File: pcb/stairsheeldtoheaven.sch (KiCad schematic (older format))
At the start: 29 parts

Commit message: schema complet
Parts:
- removed D?: LED, LEDs:LED-5MM, symbol LED-RESCUE-atxpowerboard
- removed P? (x16): CONN_01X02, symbol CONN_01X02
- removed R?: 220, Resistors_ThroughHole:Resistor_Horizontal_RM10mm, symbol R-RESCUE-atxpowerboard
- added P10, P11, P12, P13, P14, P15, P16, P17, P18, P19, P20, P21, P5, P6, P7, P8: CONN_01X02, symbol CONN_01X02
- gave numbers to parts that had none: 11
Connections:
- net A2 is gone; now on net 17: P22.2 (P2)
- net A3 is gone; now on net 18: P23.2 (P2)
- net A4 is gone; now on net 19: P24.2 (P2)
- net A5 is gone; now on net 20: P25.2 (P2)
- net 1: now also SHIELD1.0, P5.2 (P2)
- net 10: now also SHIELD1.9, P15.2 (P2)
- net 11: now also SHIELD1.10, P16.2 (P2)
- net 12: now also SHIELD1.11, P17.2 (P2)
- net 13: now also SHIELD1.12, P18.2 (P2)
- net 2: now also SHIELD1.1, P6.2 (P2)
- net 3: now also SHIELD1.2, P7.2 (P2)
- net 4: now also SHIELD1.3, P8.2 (P2)
- net 5: now also SHIELD1.4, P10.2 (P2)
- net 6: now also SHIELD1.5, P11.2 (P2)
- net 7: now also SHIELD1.6, P12.2 (P2)
- net 8: now also SHIELD1.7, P13.2 (P2)
- net 9: now also SHIELD1.8, P14.2 (P2)
- net GND: now also P22.1 (P1), P23.1 (P1), P24.1 (P1), P25.1 (P1), SHIELD1._GND (ICSP_GND), P10.1 (P1), P11.1 (P1), P12.1 (P1), P13.1 (P1), P14.1 (P1), P15.1 (P1), P16.1 (P1), P17.1 (P1), P18.1 (P1), P19.1 (P1), P20.1 (P1), P21.1 (P1), P5.1 (P1), P6.1 (P1), P7.1 (P1), P8.1 (P1)
- net clock: now also SHIELD1._SCK (ICSP_SCK)
- net data: now also SHIELD1._MOS (ICSP_MOSI)
- net 14: now reaches SHIELD1.13
- net 14: now also P19.2 (P2)
- net 15: now reaches SHIELD1.AD0
- net 15: now also P20.2 (P2)
- net 16: now reaches SHIELD1.AD1
- net 16: now also P21.2 (P2)
- net 17: now reaches SHIELD1.AD2
- net 18: now reaches SHIELD1.AD3
- net 19: now reaches SHIELD1.AD4
- net 20: now reaches SHIELD1.AD5
- net +5V renamed 5V_SB
- no-connect marks 2 -> 13
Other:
- moved on the sheet: P22, P23, P24, P25

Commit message: version1 PCB
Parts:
- JP1: footprint (none) -> Pin_Headers:Pin_Header_Straight_1x02
- P10: value CONN_01X02 -> 5; footprint (none) -> Connect:bornier2
- P11: value CONN_01X02 -> 6; footprint (none) -> Connect:bornier2
- P12: value CONN_01X02 -> 7; footprint (none) -> Connect:bornier2
- P13: value CONN_01X02 -> 8; footprint (none) -> Connect:bornier2
- P14: value CONN_01X02 -> 9; footprint (none) -> Connect:bornier2
- P15: value CONN_01X02 -> 10; footprint (none) -> Connect:bornier2
- P16: value CONN_01X02 -> 11; footprint (none) -> Connect:bornier2
- P17: value CONN_01X02 -> 12; footprint (none) -> Connect:bornier2
- P18: value CONN_01X02 -> 13; footprint (none) -> Connect:bornier2
- P19: value CONN_01X02 -> 14; footprint (none) -> Connect:bornier2
- P2: value 5V -> LED1
- P20: value CONN_01X02 -> 15; footprint (none) -> Connect:bornier2
- P21: value CONN_01X02 -> 16; footprint (none) -> Connect:bornier2
- P22: value CONN_01X02 -> 17; footprint (none) -> Connect:bornier2
- P23: value CONN_01X02 -> 18; footprint (none) -> Connect:bornier2
- P24: value CONN_01X02 -> 19; footprint (none) -> Connect:bornier2
- P25: value CONN_01X02 -> 20; footprint (none) -> Connect:bornier2
- P3: value 5V -> LED2
- P5: value CONN_01X02 -> 1; footprint (none) -> Connect:bornier2
- P6: value CONN_01X02 -> 2; footprint (none) -> Connect:bornier2
- P7: value CONN_01X02 -> 3; footprint (none) -> Connect:bornier2
- P8: value CONN_01X02 -> 4; footprint (none) -> Connect:bornier2
- SHIELD1: footprint (none) -> JbLb_lib:ARDUINO_SHIELD_R3
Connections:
- net GND: now also SHIELD1.GND3
- no-connect marks 13 -> 12
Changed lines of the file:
@@
 F 0 "SHIELD1" H 2100 3500 60  0000 C CNN
 F 1 "ARDUINO_SHIELD_R3" H 2300 3300 60  0000 C CNN
-F 2 "" H 2450 2300 60  0000 C CNN
+F 2 "JbLb_lib:ARDUINO_SHIELD_R3" H 2450 2300 60  0001 C CNN
 F 3 "" H 2450 2300 60  0000 C CNN
 	1    2450 2300
@@
 P 10525 1300
 F 0 "P22" H 10525 1450 50  0000 C CNN
-F 1 "CONN_01X02" V 10625 1300 50  0000 C CNN
-F 2 "" H 10525 1300 60  0000 C CNN
+F 1 "17" V 10625 1300 50  0000 C CNN
+F 2 "Connect:bornier2" H 10525 1300 60  0001 C CNN
 F 3 "" H 10525 1300 60  0000 C CNN
 	1    10525 1300
@@
 P 10525 1850
 F 0 "P23" H 10525 2000 50  0000 C CNN
-F 1 "CONN_01X02" V 10625 1850 50  0000 C CNN
-F 2 "" H 10525 1850 60  0000 C CNN
+F 1 "18" V 10625 1850 50  0000 C CNN
+F 2 "Connect:bornier2" H 10525 1850 60  0001 C CNN
 F 3 "" H 10525 1850 60  0000 C CNN
 	1    10525 1850
@@
 P 10525 2400
 F 0 "P24" H 10525 2550 50  0000 C CNN
-F 1 "CONN_01X02" V 10625 2400 50  0000 C CNN
-F 2 "" H 10525 2400 60  0000 C CNN
+F 1 "19" V 10625 2400 50  0000 C CNN
+F 2 "Connect:bornier2" H 10525 2400 60  0001 C CNN
 F 3 "" H 10525 2400 60  0000 C CNN
 	1    10525 2400
@@
 P 10525 2950
 F 0 "P25" H 10525 3100 50  0000 C CNN
-F 1 "CONN_01X02" V 10625 2950 50  0000 C CNN
-F 2 "" H 10525 2950 60  0000 C CNN
+F 1 "20" V 10625 2950 50  0000 C CNN
+F 2 "Connect:bornier2" H 10525 2950 60  0001 C CNN
 F 3 "" H 10525 2950 60  0000 C CNN
 	1    10525 2950
@@
 F 0 "JP1" H 4450 4750 50  0000 C CNN
 F 1 "JUMPER" H 4450 4520 50  0000 C CNN
-F 2 "" H 4450 4600 60  0000 C CNN
+F 2 "Pin_Headers:Pin_Header_Straight_1x02" H 4450 4600 60  0001 C CNN
 F 3 "" H 4450 4600 60  0000 C CNN
 	1    4450 4600
@@
 P 5250 3950
 F 0 "P2" V 5200 3950 40  0000 C CNN
-F 1 "5V" V 5300 3950 40  0000 C CNN
+F 1 "LED1" V 5300 3950 40  0000 C CNN
 F 2 "Connect:bornier2" H 5250 3950 60  0001 C CNN
 F 3 "" H 5250 3950 60  0000 C CNN
@@
 P 5600 3950
 F 0 "P3" V 5550 3950 40  0000 C CNN
-F 1 "5V" V 5650 3950 40  0000 C CNN
+F 1 "LED2" V 5650 3950 40  0000 C CNN
 F 2 "Connect:bornier2" H 5600 3950 60  0001 C CNN
 F 3 "" H 5600 3950 60  0000 C CNN
@@
 P 9825 1300
 F 0 "P18" H 9825 1450 50  0000 C CNN
-F 1 "CONN_01X02" V 9925 1300 50  0000 C CNN
-F 2 "" H 9825 1300 60  0000 C CNN
+F 1 "13" V 9925 1300 50  0000 C CNN
+F 2 "Connect:bornier2" H 9825 1300 60  0001 C CNN
 F 3 "" H 9825 1300 60  0000 C CNN
 	1    9825 1300
@@
 P 9825 1850
 F 0 "P19" H 9825 2000 50  0000 C CNN
-F 1 "CONN_01X02" V 9925 1850 50  0000 C CNN
-F 2 "" H 9825 1850 60  0000 C CNN
+F 1 "14" V 9925 1850 50  0000 C CNN
+F 2 "Connect:bornier2" H 9825 1850 60  0001 C CNN
 F 3 "" H 9825 1850 60  0000 C CNN
 	1    9825 1850
@@
 P 9825 2400
 F 0 "P20" H 9825 2550 50  0000 C CNN
-F 1 "CONN_01X02" V 9925 2400 50  0000 C CNN
-F 2 "" H 9825 2400 60  0000 C CNN
+F 1 "15" V 9925 2400 50  0000 C CNN
+F 2 "Connect:bornier2" H 9825 2400 60  0001 C CNN
 F 3 "" H 9825 2400 60  0000 C CNN
 	1    9825 2400
@@
 P 9825 2950
 F 0 "P21" H 9825 3100 50  0000 C CNN
-F 1 "CONN_01X02" V 9925 2950 50  0000 C CNN
-F 2 "" H 9825 2950 60  0000 C CNN
+F 1 "16" V 9925 2950 50  0000 C CNN
+F 2 "Connect:bornier2" H 9825 2950 60  0001 C CNN
 F 3 "" H 9825 2950 60  0000 C CNN
 	1    9825 2950
@@
 P 9100 1300
 F 0 "P14" H 9100 1450 50  0000 C CNN
-F 1 "CONN_01X02" V 9200 1300 50  0000 C CNN
-F 2 "" H 9100 1300 60  0000 C CNN
+F 1 "9" V 9200 1300 50  0000 C CNN
+F 2 "Connect:bornier2" H 9100 1300 60  0001 C CNN
 F 3 "" H 9100 1300 60  0000 C CNN
 	1    9100 1300
@@
 P 9100 1850
 F 0 "P15" H 9100 2000 50  0000 C CNN
-F 1 "CONN_01X02" V 9200 1850 50  0000 C CNN
-F 2 "" H 9100 1850 60  0000 C CNN
+F 1 "10" V 9200 1850 50  0000 C CNN
+F 2 "Connect:bornier2" H 9100 1850 60  0001 C CNN
 F 3 "" H 9100 1850 60  0000 C CNN
 	1    9100 1850
@@
 P 9100 2400
 F 0 "P16" H 9100 2550 50  0000 C CNN
-F 1 "CONN_01X02" V 9200 2400 50  0000 C CNN
-F 2 "" H 9100 2400 60  0000 C CNN
+F 1 "11" V 9200 2400 50  0000 C CNN
+F 2 "Connect:bornier2" H 9100 2400 60  0001 C CNN
 F 3 "" H 9100 2400 60  0000 C CNN
 	1    9100 2400
@@
 P 9100 2950
 F 0 "P17" H 9100 3100 50  0000 C CNN
-F 1 "CONN_01X02" V 9200 2950 50  0000 C CNN
-F 2 "" H 9100 2950 60  0000 C CNN
+F 1 "12" V 9200 2950 50  0000 C CNN
+F 2 "Connect:bornier2" H 9100 2950 60  0001 C CNN
 F 3 "" H 9100 2950 60  0000 C CNN
 	1    9100 2950
@@
 P 8400 1300
 F 0 "P10" H 8400 1450 50  0000 C CNN
-F 1 "CONN_01X02" V 8500 1300 50  0000 C CNN
-F 2 "" H 8400 1300 60  0000 C CNN
+F 1 "5" V 8500 1300 50  0000 C CNN
+F 2 "Connect:bornier2" H 8400 1300 60  0001 C CNN
 F 3 "" H 8400 1300 60  0000 C CNN
 	1    8400 1300
@@
 P 8400 1850
 F 0 "P11" H 8400 2000 50  0000 C CNN
-F 1 "CONN_01X02" V 8500 1850 50  0000 C CNN
-F 2 "" H 8400 1850 60  0000 C CNN
+F 1 "6" V 8500 1850 50  0000 C CNN
+F 2 "Connect:bornier2" H 8400 1850 60  0001 C CNN
 F 3 "" H 8400 1850 60  0000 C CNN
 	1    8400 1850
@@
 P 8400 2400
 F 0 "P12" H 8400 2550 50  0000 C CNN
-F 1 "CONN_01X02" V 8500 2400 50  0000 C CNN
-F 2 "" H 8400 2400 60  0000 C CNN
+F 1 "7" V 8500 2400 50  0000 C CNN
+F 2 "Connect:bornier2" H 8400 2400 60  0001 C CNN
 F 3 "" H 8400 2400 60  0000 C CNN
 	1    8400 2400
@@
 P 8400 2950
 F 0 "P13" H 8400 3100 50  0000 C CNN
-F 1 "CONN_01X02" V 8500 2950 50  0000 C CNN
-F 2 "" H 8400 2950 60  0000 C CNN
+F 1 "8" V 8500 2950 50  0000 C CNN
+F 2 "Connect:bornier2" H 8400 2950 60  0001 C CNN
 F 3 "" H 8400 2950 60  0000 C CNN
 	1    8400 2950
@@
 P 7575 1300
 F 0 "P5" H 7575 1450 50  0000 C CNN
-F 1 "CONN_01X02" V 7675 1300 50  0000 C CNN
-F 2 "" H 7575 1300 60  0000 C CNN
+F 1 "1" V 7675 1300 50  0000 C CNN
+F 2 "Connect:bornier2" H 7575 1300 60  0001 C CNN
 F 3 "" H 7575 1300 60  0000 C CNN
 	1    7575 1300
@@
 P 7575 1850
 F 0 "P6" H 7575 2000 50  0000 C CNN
-F 1 "CONN_01X02" V 7675 1850 50  0000 C CNN
-F 2 "" H 7575 1850 60  0000 C CNN
+F 1 "2" V 7675 1850 50  0000 C CNN
+F 2 "Connect:bornier2" H 7575 1850 60  0001 C CNN
 F 3 "" H 7575 1850 60  0000 C CNN
 	1    7575 1850
@@
 P 7575 2400
 F 0 "P7" H 7575 2550 50  0000 C CNN
-F 1 "CONN_01X02" V 7675 2400 50  0000 C CNN
-F 2 "" H 7575 2400 60  0000 C CNN
+F 1 "3" V 7675 2400 50  0000 C CNN
+F 2 "Connect:bornier2" H 7575 2400 60  0001 C CNN
 F 3 "" H 7575 2400 60  0000 C CNN
 	1    7575 2400
@@
 P 7575 2950
 F 0 "P8" H 7575 3100 50  0000 C CNN
-F 1 "CONN_01X02" V 7675 2950 50  0000 C CNN
-F 2 "" H 7575 2950 60  0000 C CNN
+F 1 "4" V 7675 2950 50  0000 C CNN
+F 2 "Connect:bornier2" H 7575 2950 60  0001 C CNN
 F 3 "" H 7575 2950 60  0000 C CNN
 	1    7575 2950
@@
 NoConn ~ 2250 3500
 NoConn ~ 2550 3500
-NoConn ~ 3400 1600
 NoConn ~ 3400 1500
 NoConn ~ 3400 1400
 NoConn ~ 3400 1300
 NoConn ~ 4500 2550
+$Comp
+L GND-RESCUE-atxpowerboard #PWR?
+U 1 1 561587CE
+P 3550 1600
+F 0 "#PWR?" H 3550 1600 30  0001 C CNN
+F 1 "GND" H 3550 1530 30  0001 C CNN
+F 2 "" H 3550 1600 60  0000 C CNN
+F 3 "" H 3550 1600 60  0000 C CNN
+	1    3550 1600
+	0    -1   -1   0
+$EndComp
+Wire Wire Line
+	3400 1600 3550 1600
 $EndSCHEMATC

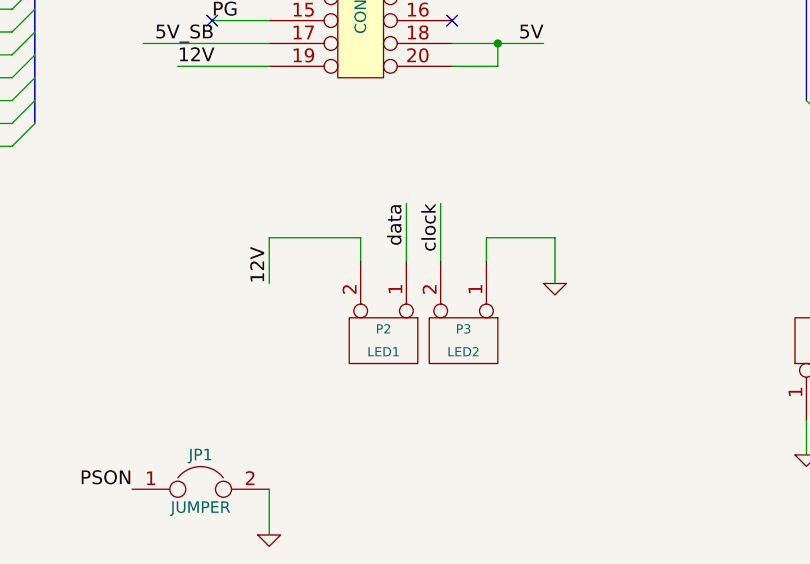
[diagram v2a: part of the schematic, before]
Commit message: simplification connection LED
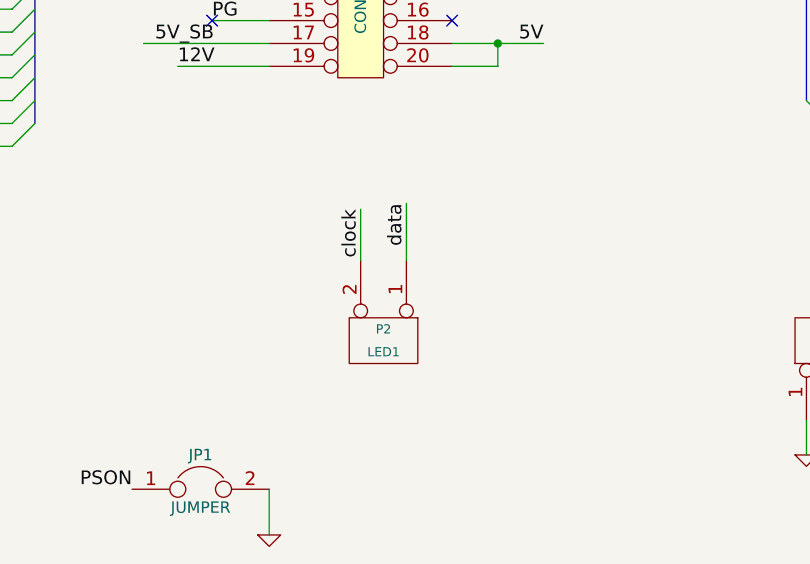
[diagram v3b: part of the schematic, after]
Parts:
- removed P3: LED2, Connect:bornier2, symbol CONN_2
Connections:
- net 12V: no longer P2.2 (PM)
- net clock: now also P2.2 (PM)
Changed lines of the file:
@@
 EESchema Schematic File Version 2
+LIBS:arduino_shieldsNCL
 LIBS:power
 LIBS:device
@@
 LIBS:contrib
 LIBS:valves
+LIBS:crumpschemes
 LIBS:stairsheeldtoheaven-cache
 EELAYER 25 0
@@
 	0    1    1    0
 $EndComp
-$Comp
-L CONN_2 P3
-U 1 1 5614A1B8
-P 5600 3950
-F 0 "P3" V 5550 3950 40  0000 C CNN
-F 1 "LED2" V 5650 3950 40  0000 C CNN
-F 2 "Connect:bornier2" H 5600 3950 60  0001 C CNN
-F 3 "" H 5600 3950 60  0000 C CNN
-	1    5600 3950
-	0    1    1    0
-$EndComp
-$Comp
-L GND-RESCUE-atxpowerboard #PWR07
-U 1 1 5614A468
-P 6000 3700
-F 0 "#PWR07" H 6000 3700 30  0001 C CNN
-F 1 "GND" H 6000 3630 30  0001 C CNN
-F 2 "" H 6000 3700 60  0000 C CNN
-F 3 "" H 6000 3700 60  0000 C CNN
-	1    6000 3700
-	1    0    0    -1
-$EndComp
-Text Label 4750 3700 1    60   ~ 0
-12V
 Text Label 5350 3350 3    60   ~ 0
 data
-Text Label 5500 3350 3    60   ~ 0
+Text Label 5150 3375 3    60   ~ 0
 clock
 Text Label 2650 3500 3    60   ~ 0
@@
 clock
 $Comp
-L GND-RESCUE-atxpowerboard #PWR08
+L GND-RESCUE-atxpowerboard #PWR07
 U 1 1 5614DF3A
 P 2750 3650
-F 0 "#PWR08" H 2750 3650 30  0001 C CNN
+F 0 "#PWR07" H 2750 3650 30  0001 C CNN
 F 1 "GND" H 2750 3580 30  0001 C CNN
 F 2 "" H 2750 3650 60  0000 C CNN
@@
 	1500 2300 1100 2300
 Connection ~ 1100 2300
-Wire Wire Line
-	6000 3700 6000 3500
-Wire Wire Line
-	6000 3500 5700 3500
-Wire Wire Line
-	5700 3500 5700 3600
-Wire Wire Line
-	4750 3700 4750 3500
-Wire Wire Line
-	4750 3500 5150 3500
-Wire Wire Line
-	5150 3500 5150 3600
-Wire Wire Line
-	5500 3600 5500 3350
 Wire Wire Line
 	5350 3600 5350 3350
@@
 Connection ~ 7175 1000
 $Comp
-L GND-RESCUE-atxpowerboard #PWR09
+L GND-RESCUE-atxpowerboard #PWR08
 U 1 1 561545E5
 P 6850 1250
-F 0 "#PWR09" H 6850 1250 30  0001 C CNN
+F 0 "#PWR08" H 6850 1250 30  0001 C CNN
 F 1 "GND" H 6850 1180 30  0001 C CNN
 F 2 "" H 6850 1250 60  0000 C CNN
@@
 NoConn ~ 4500 2550
 $Comp
-L GND-RESCUE-atxpowerboard #PWR?
+L GND-RESCUE-atxpowerboard #PWR09
 U 1 1 561587CE
 P 3550 1600
-F 0 "#PWR?" H 3550 1600 30  0001 C CNN
+F 0 "#PWR09" H 3550 1600 30  0001 C CNN
 F 1 "GND" H 3550 1530 30  0001 C CNN
 F 2 "" H 3550 1600 60  0000 C CNN
@@
 Wire Wire Line
 	3400 1600 3550 1600
+Wire Wire Line
+	5150 3600 5150 3375
 $EndSCHEMATC
